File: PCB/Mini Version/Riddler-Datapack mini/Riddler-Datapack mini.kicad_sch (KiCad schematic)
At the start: 0 parts

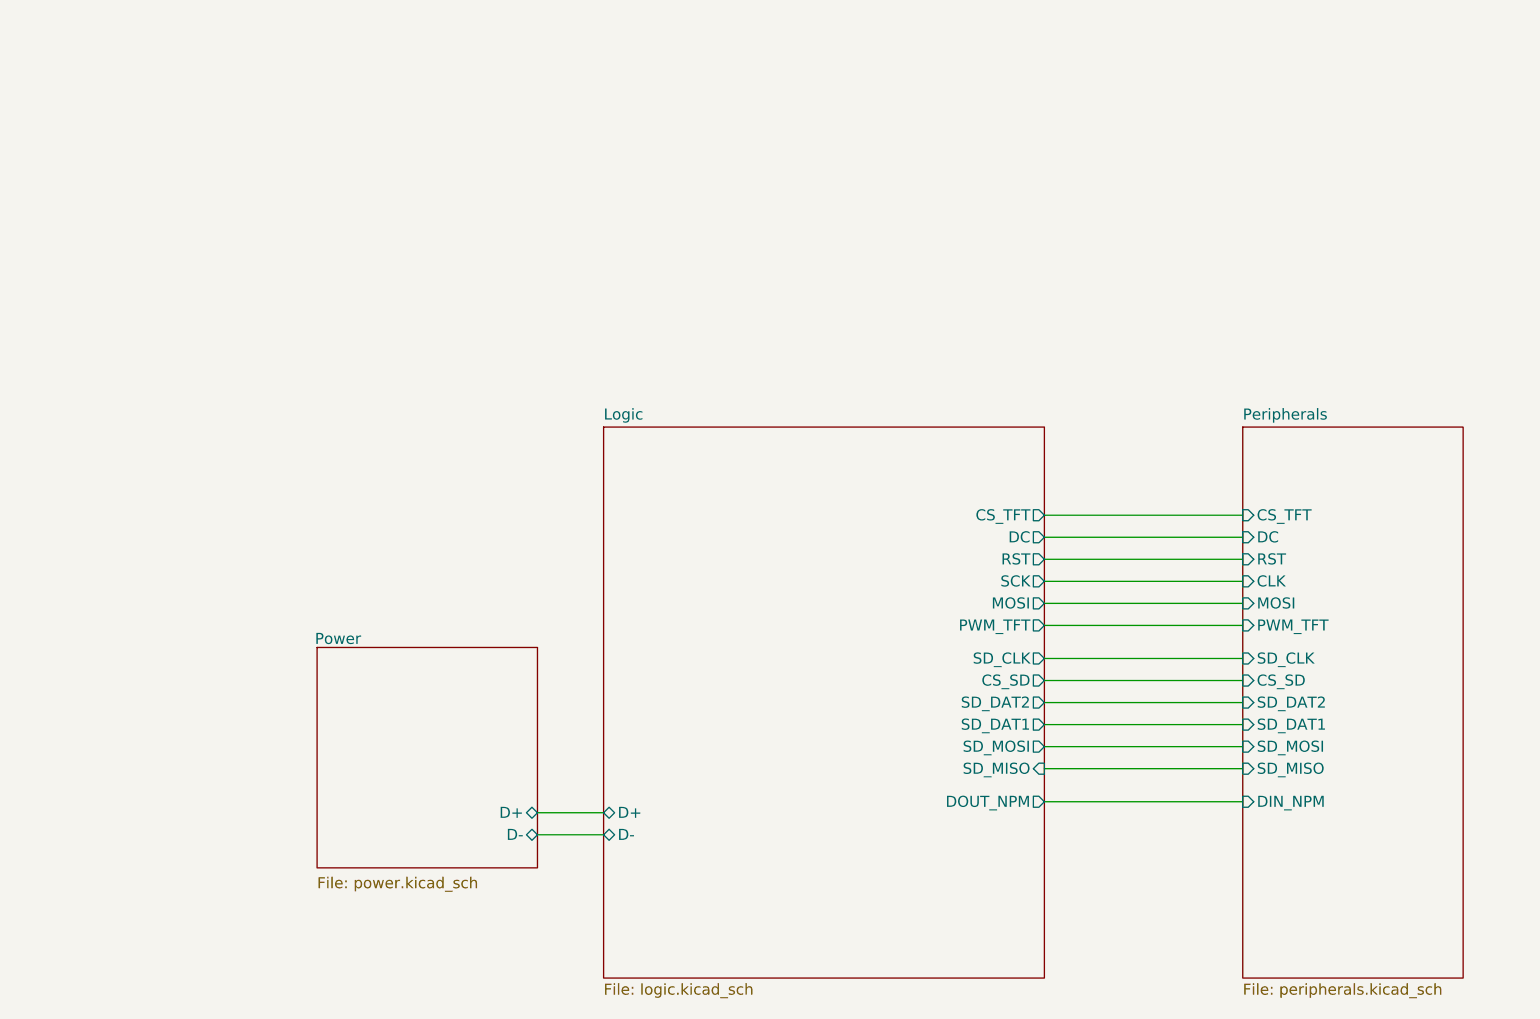
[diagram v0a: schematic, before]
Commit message: feat(hardware): complete 4-layer PCB routing for Mini Datapack prop and add 3D exports
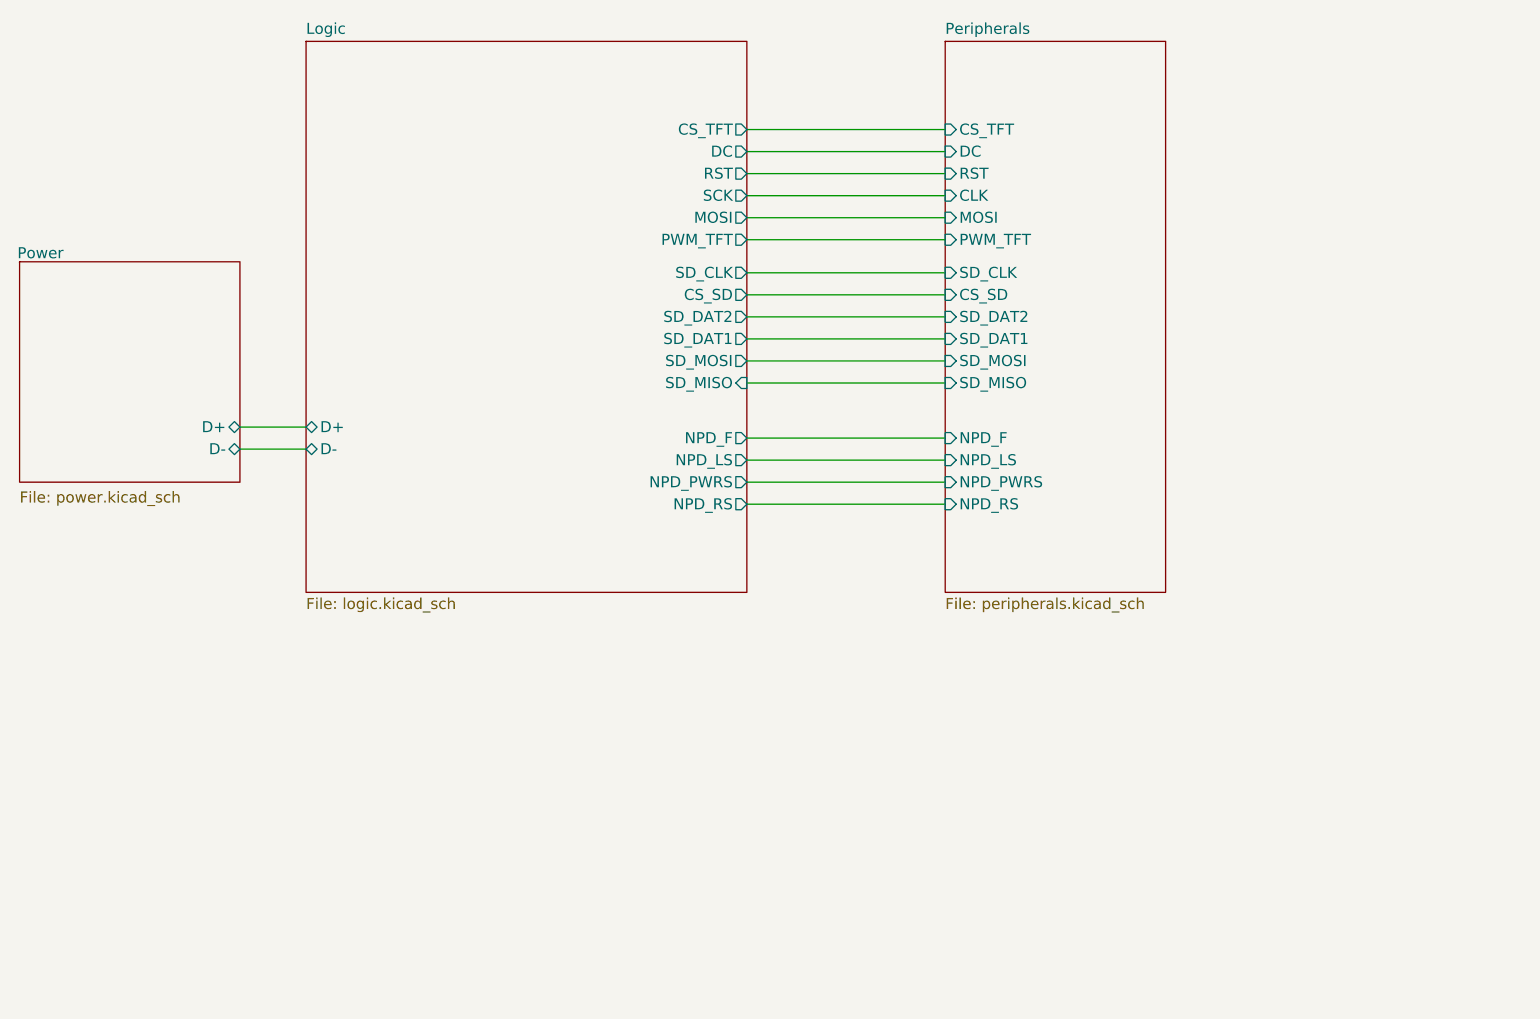
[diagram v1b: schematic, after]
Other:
- sheet Logic ports: added NPD_F, NPD_LS, NPD_PWRS, NPD_RS; removed DOUT_NPM
- sheet Peripherals ports: added NPD_F, NPD_LS, NPD_PWRS, NPD_RS; removed DIN_NPM

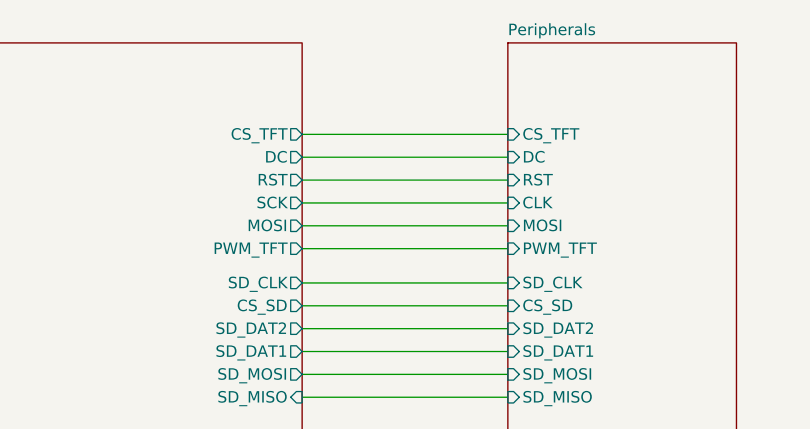
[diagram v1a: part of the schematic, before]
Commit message: v1.1: update Mini Datapack with repositioned USB-C, relief vias, and v1p1 exports
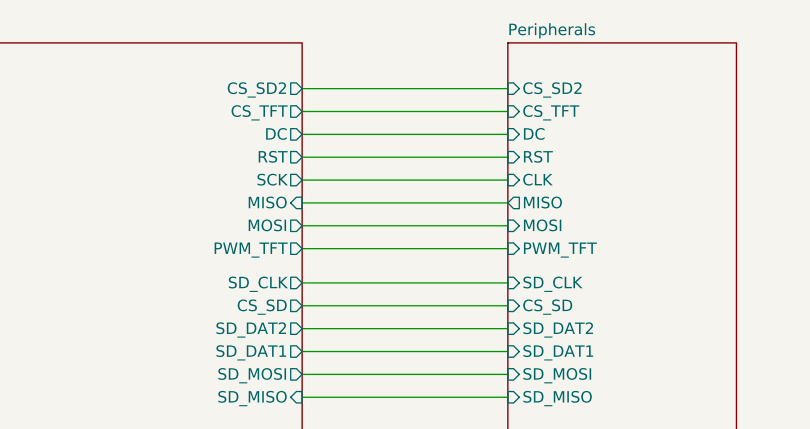
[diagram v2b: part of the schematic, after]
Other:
- sheet Logic ports: added CS_SD2, MISO; removed none
- sheet Peripherals ports: added CS_SD2, MISO; removed none
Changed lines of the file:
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@@
+	(wire
+		(pts
+			(xy 118.11 36.83) (xy 140.97 36.83)
+		)
+		(stroke
+			(width 0)
+			(type default)
+		)
+	)
 	(wire
 		(pts
@@
 	(wire
 		(pts
+			(xy 118.11 41.91) (xy 140.97 41.91)
+		)
+		(stroke
+			(width 0)
+			(type default)
+		)
+	)
+	(wire
+		(pts
+			(xy 59.69 78.74) (xy 67.31 78.74)
+		)
+		(stroke
+			(width 0)
+			(type default)
+		)
+	)
+	(wire
+		(pts
+			(xy 118.11 49.53) (xy 140.97 49.53)
+		)
+		(stroke
+			(width 0)
+			(type default)
+		)
+	)
+	(wire
+		(pts
+			(xy 118.11 80.01) (xy 140.97 80.01)
+		)
+		(stroke
+			(width 0)
+			(type default)
+		)
+	)
+	(wire
+		(pts
+			(xy 118.11 52.07) (xy 140.97 52.07)
+		)
+		(stroke
+			(width 0)
+			(type default)
+		)
+	)
+	(wire
+		(pts
+			(xy 118.11 39.37) (xy 140.97 39.37)
+		)
+		(stroke
+			(width 0)
+			(type default)
+		)
+	)
+	(wire
+		(pts
+			(xy 118.11 66.04) (xy 140.97 66.04)
+		)
+		(stroke
+			(width 0)
+			(type default)
+		)
+	)
+	(wire
+		(pts
+			(xy 118.11 63.5) (xy 140.97 63.5)
+		)
+		(stroke
+			(width 0)
+			(type default)
+		)
+	)
+	(wire
+		(pts
 			(xy 118.11 44.45) (xy 140.97 44.45)
 		)
@@
 	(wire
 		(pts
-			(xy 59.69 78.74) (xy 67.31 78.74)
-		)
-		(stroke
-			(width 0)
-			(type default)
-		)
-	)
-	(wire
-		(pts
-			(xy 118.11 80.01) (xy 140.97 80.01)
-		)
-		(stroke
-			(width 0)
-			(type default)
-		)
-	)
-	(wire
-		(pts
-			(xy 118.11 52.07) (xy 140.97 52.07)
-		)
-		(stroke
-			(width 0)
-			(type default)
-		)
-	)
-	(wire
-		(pts
-			(xy 118.11 41.91) (xy 140.97 41.91)
-		)
-		(stroke
-			(width 0)
-			(type default)
-		)
-	)
-	(wire
-		(pts
-			(xy 118.11 66.04) (xy 140.97 66.04)
-		)
-		(stroke
-			(width 0)
-			(type default)
-		)
-	)
-	(wire
-		(pts
-			(xy 118.11 63.5) (xy 140.97 63.5)
-		)
-		(stroke
-			(width 0)
-			(type default)
-		)
-	)
-	(wire
-		(pts
 			(xy 118.11 46.99) (xy 140.97 46.99)
-		)
-		(stroke
-			(width 0)
-			(type default)
-		)
-	)
-	(wire
-		(pts
-			(xy 118.11 49.53) (xy 140.97 49.53)
 		)
 		(stroke
@@
 		)
 		(pin "CS_TFT" output
+			(at 118.11 39.37 0)
+			(effects
+				(font
+					(size 1.27 1.27)
+				)
+				(justify right)
+			)
+		)
+		(pin "DC" output
 			(at 118.11 41.91 0)
-			(effects
-				(font
-					(size 1.27 1.27)
-				)
-				(justify right)
-			)
-		)
-		(pin "DC" output
-			(at 118.11 44.45 0)
 			(effects
 				(font
@@
 		)
 		(pin "RST" output
+			(at 118.11 44.45 0)
+			(effects
+				(font
+					(size 1.27 1.27)
+				)
+				(justify right)
+			)
+		)
+		(pin "SCK" output
 			(at 118.11 46.99 0)
-			(effects
-				(font
-					(size 1.27 1.27)
-				)
-				(justify right)
-			)
-		)
-		(pin "SCK" output
-			(at 118.11 49.53 0)
 			(effects
 				(font
@@
 		(pin "NPD_RS" output
 			(at 118.11 85.09 0)
+			(effects
+				(font
+					(size 1.27 1.27)
+				)
+				(justify right)
+			)
+		)
+		(pin "CS_SD2" output
+			(at 118.11 36.83 0)
+			(effects
+				(font
+					(size 1.27 1.27)
+				)
+				(justify right)
+			)
+		)
+		(pin "MISO" input
+			(at 118.11 49.53 0)
 			(effects
 				(font
@@
 		)
 		(pin "CLK" input
-			(at 140.97 49.53 180)
+			(at 140.97 46.99 180)
 			(effects
 				(font
@@
 		)
 		(pin "CS_TFT" input
+			(at 140.97 39.37 180)
+			(effects
+				(font
+					(size 1.27 1.27)
+				)
+				(justify left)
+			)
+		)
+		(pin "DC" input
 			(at 140.97 41.91 180)
-			(effects
-				(font
-					(size 1.27 1.27)
-				)
-				(justify left)
-			)
-		)
-		(pin "DC" input
-			(at 140.97 44.45 180)
 			(effects
 				(font
@@
 		)
 		(pin "RST" input
-			(at 140.97 46.99 180)
+			(at 140.97 44.45 180)
 			(effects
 				(font
@@
 			(effects
 				(font
+					(size 1.27 1.27)
+				)
+				(justify left)
+			)
+		)
+		(pin "CS_SD2" input
+			(at 140.97 36.83 180)
+			(effects
+				(font
+					(size 1.27 1.27)
+				)
+				(justify left)
+			)
+		)
+		(pin "MISO" output
+			(at 140.97 49.53 180)
+			(effects
+				(font
